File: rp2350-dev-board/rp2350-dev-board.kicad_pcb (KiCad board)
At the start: 2 copper layers, 40 parts, among them J1 USB_C_Receptacle_USB2.0_14P, J10 M1, J11 M1, J12 M1, J13 PWR_IN, J14 SWD, J2 M_EN, J3 HDMI_A, J8 1.47_IPS_LCD, J9 TMC_Volt_Select, SW1 BTN1, SW2 BTN1, SW3 BTN1, SW4 BTN1, SW5 BTN1, U4 L7805

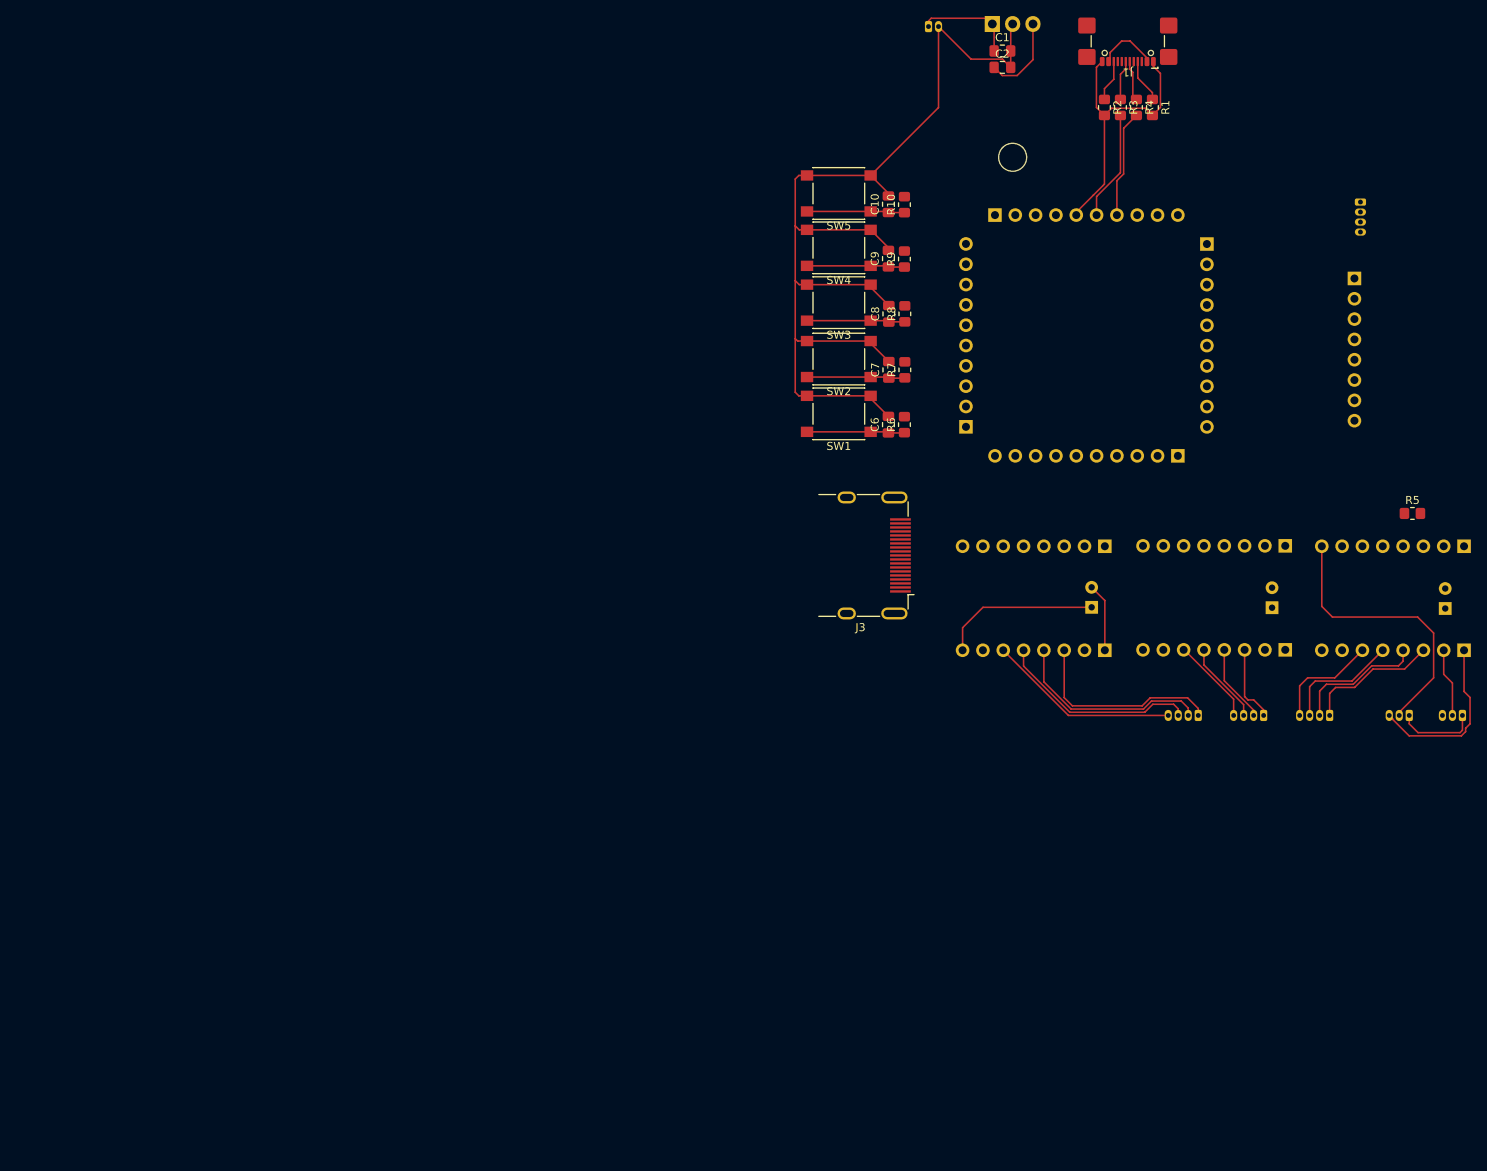
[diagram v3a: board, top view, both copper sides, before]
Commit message: feat(rp2350-devboard): copying tmc2209 and rp2350a-tempel into rp2350a devboard
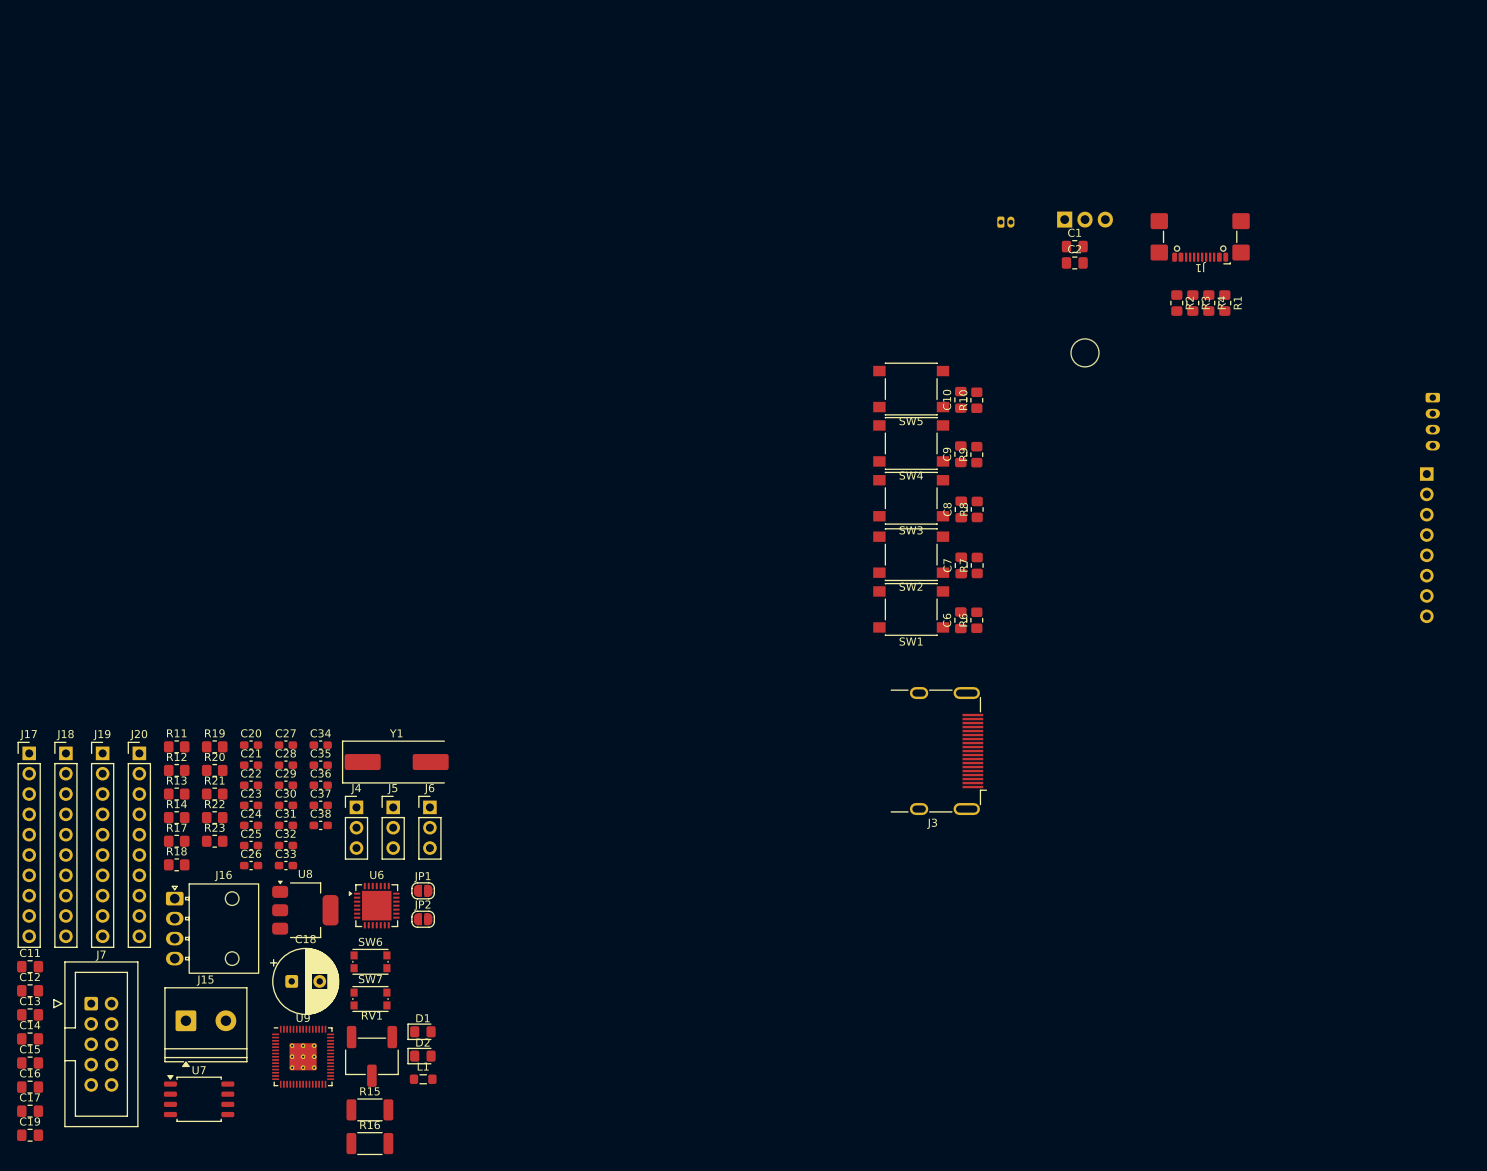
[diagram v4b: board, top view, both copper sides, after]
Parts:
- removed C3, C4, C5: 100uF, Capacitor_THT:CP_Radial_D6.3mm_P2.50mm
- removed J10, J11, J12: M1, Connector_Hirose:Hirose_DF13-04P-1.25DSA_1x04_P1.25mm_Vertical
- removed J2: M_EN, Connector_Hirose:Hirose_DF13-03P-1.25DSA_1x03_P1.25mm_Vertical
- removed J9: TMC_Volt_Select, Connector_Hirose:Hirose_DF13-03P-1.25DSA_1x03_P1.25mm_Vertical
- removed R5: 1K, Resistor_SMD:R_0805_2012Metric_Pad1.20x1.40mm_HandSolder
- removed U1, U2, U3: ~, rp2350-tempel-lib:TMC2209_MKS_V2
- removed U5: ~, rp2350-tempel-lib:RP2350_Tempel_Footprint
- added C11: 100nF, Capacitor_SMD:C_0805_2012Metric_Pad1.18x1.45mm_HandSolder, F.Cu at (32.7, 148.7)
- added C12: 100nF, Capacitor_SMD:C_0805_2012Metric_Pad1.18x1.45mm_HandSolder, F.Cu at (32.7, 151.7)
- added C13: 100nF, Capacitor_SMD:C_0805_2012Metric_Pad1.18x1.45mm_HandSolder, F.Cu at (32.7, 154.7)
- added C14: 100nF, Capacitor_SMD:C_0805_2012Metric_Pad1.18x1.45mm_HandSolder, F.Cu at (32.7, 157.7)
- added C15: 22nF/50V, Capacitor_SMD:C_0805_2012Metric_Pad1.18x1.45mm_HandSolder, F.Cu at (32.7, 160.7)
- added C16: 4.7uF, Capacitor_SMD:C_0805_2012Metric_Pad1.18x1.45mm_HandSolder, F.Cu at (32.7, 163.8)
- added C17: 4.7uF, Capacitor_SMD:C_0805_2012Metric_Pad1.18x1.45mm_HandSolder, F.Cu at (32.7, 166.8)
- added C18: 100uF, Capacitor_THT:CP_Radial_D8.0mm_P3.50mm, F.Cu at (65.4, 150.5)
- added C19: 2.2uF to 4.7uF/50V, Capacitor_SMD:C_0805_2012Metric_Pad1.18x1.45mm_HandSolder, F.Cu at (32.7, 169.8)
- added C20: 22uF, Capacitor_SMD:C_0603_1608Metric_Pad1.08x0.95mm_HandSolder, F.Cu at (60.3, 121.0)
- added C21: 100nF, Capacitor_SMD:C_0603_1608Metric_Pad1.08x0.95mm_HandSolder, F.Cu at (60.3, 123.5)
- added C22: 22uF, Capacitor_SMD:C_0603_1608Metric_Pad1.08x0.95mm_HandSolder, F.Cu at (60.3, 126.0)
- added C23: 12pF, Capacitor_SMD:C_0603_1608Metric_Pad1.08x0.95mm_HandSolder, F.Cu at (60.3, 128.5)
- added C24: 4.7uF, Capacitor_SMD:C_0603_1608Metric_Pad1.08x0.95mm_HandSolder, F.Cu at (60.3, 131.0)
- added C25: 4.7uF, Capacitor_SMD:C_0603_1608Metric_Pad1.08x0.95mm_HandSolder, F.Cu at (60.3, 133.6)
- added C26: 12pF, Capacitor_SMD:C_0603_1608Metric_Pad1.08x0.95mm_HandSolder, F.Cu at (60.3, 136.1)
- added C27: 4.7uF, Capacitor_SMD:C_0603_1608Metric_Pad1.08x0.95mm_HandSolder, F.Cu at (64.6, 121.0)
- added C28: 1uF, Capacitor_SMD:C_0603_1608Metric_Pad1.08x0.95mm_HandSolder, F.Cu at (64.6, 123.5)
- added C29: 4.7uF, Capacitor_SMD:C_0603_1608Metric_Pad1.08x0.95mm_HandSolder, F.Cu at (64.6, 126.0)
- added C30: 100nF, Capacitor_SMD:C_0603_1608Metric_Pad1.08x0.95mm_HandSolder, F.Cu at (64.6, 128.5)
- added C31: 100nF, Capacitor_SMD:C_0603_1608Metric_Pad1.08x0.95mm_HandSolder, F.Cu at (64.6, 131.0)
- added C32: 100nF, Capacitor_SMD:C_0603_1608Metric_Pad1.08x0.95mm_HandSolder, F.Cu at (64.6, 133.6)
- added C33: 100nF, Capacitor_SMD:C_0603_1608Metric_Pad1.08x0.95mm_HandSolder, F.Cu at (64.6, 136.1)
- added C34: 100nF, Capacitor_SMD:C_0603_1608Metric_Pad1.08x0.95mm_HandSolder, F.Cu at (69.0, 121.0)
- added C35: 100nF, Capacitor_SMD:C_0603_1608Metric_Pad1.08x0.95mm_HandSolder, F.Cu at (69.0, 123.5)
- added C36: 100nF, Capacitor_SMD:C_0603_1608Metric_Pad1.08x0.95mm_HandSolder, F.Cu at (69.0, 126.0)
- added C37: 100nF, Capacitor_SMD:C_0603_1608Metric_Pad1.08x0.95mm_HandSolder, F.Cu at (69.0, 128.5)
- added C38: 2u2F, Capacitor_SMD:C_0603_1608Metric_Pad1.08x0.95mm_HandSolder, F.Cu at (69.0, 131.0)
- added D1: DIAG, LED_SMD:LED_0805_2012Metric_Pad1.15x1.40mm_HandSolder, F.Cu at (81.8, 156.8)
- added D2: red, LED_SMD:LED_0805_2012Metric_Pad1.15x1.40mm_HandSolder, F.Cu at (81.8, 159.9)
- added J15: TMC2209_VIN, TerminalBlock_Phoenix:TerminalBlock_Phoenix_PT-1,5-2-5.0-H_1x02_P5.00mm_Horizontal, F.Cu at (52.1, 155.5)
- added J16: TMC2209_Conn, Connector_Molex:Molex_Nano-Fit_105313-xx04_1x04_P2.50mm_Horizontal, F.Cu at (50.7, 140.2)
- added J17: Conn_West, Connector_PinHeader_2.54mm:PinHeader_1x10_P2.54mm_Vertical, F.Cu at (32.5, 122.0)
- added J18: Conn_North, Connector_PinHeader_2.54mm:PinHeader_1x10_P2.54mm_Vertical, F.Cu at (37.1, 122.0)
- added J19: Conn_South, Connector_PinHeader_2.54mm:PinHeader_1x10_P2.54mm_Vertical, F.Cu at (41.7, 122.0)
- added J20: Conn_East, Connector_PinHeader_2.54mm:PinHeader_1x10_P2.54mm_Vertical, F.Cu at (46.3, 122.0)
- added J4: MS1, Connector_PinHeader_2.54mm:PinHeader_1x03_P2.54mm_Vertical, F.Cu at (73.5, 128.8)
- added J5: MS2, Connector_PinHeader_2.54mm:PinHeader_1x03_P2.54mm_Vertical, F.Cu at (78.0, 128.8)
- added J6: Spread, Connector_PinHeader_2.54mm:PinHeader_1x03_P2.54mm_Vertical, F.Cu at (82.6, 128.8)
- added J7: DriverConn, Connector_IDC:IDC-Header_2x05_P2.54mm_Vertical, F.Cu at (40.3, 153.3)
- added JP1: BRA, Jumper:SolderJumper-2_P1.3mm_Open_RoundedPad1.0x1.5mm, F.Cu at (81.8, 139.2)
- added JP2: BRB, Jumper:SolderJumper-2_P1.3mm_Open_RoundedPad1.0x1.5mm, F.Cu at (81.8, 142.8)
- added L1: 3.3uH, Inductor_SMD:L_0805_2012Metric_Pad1.05x1.20mm_HandSolder, F.Cu at (81.8, 162.8)
- added R11: 20K, Resistor_SMD:R_0805_2012Metric_Pad1.20x1.40mm_HandSolder, F.Cu at (51.0, 121.2)
- added R12: 100K, Resistor_SMD:R_0805_2012Metric_Pad1.20x1.40mm_HandSolder, F.Cu at (51.0, 124.2)
- added R13: 220, Resistor_SMD:R_0805_2012Metric_Pad1.20x1.40mm_HandSolder, F.Cu at (51.0, 127.1)
- added R14: 100K, Resistor_SMD:R_0805_2012Metric_Pad1.20x1.40mm_HandSolder, F.Cu at (51.0, 130.1)
- added R15: 120m 1W 2010, Resistor_SMD:R_2010_5025Metric, F.Cu at (75.1, 166.6)
- added R16: 120m 1W 2010, Resistor_SMD:R_2010_5025Metric, F.Cu at (75.1, 170.8)
- added R17: 10K, Resistor_SMD:R_0805_2012Metric_Pad1.20x1.40mm_HandSolder, F.Cu at (51.0, 133.0)
- added R18: 2K2, Resistor_SMD:R_0805_2012Metric_Pad1.20x1.40mm_HandSolder, F.Cu at (51.0, 136.0)
- added R19: 1K, Resistor_SMD:R_0805_2012Metric_Pad1.20x1.40mm_HandSolder, F.Cu at (55.7, 121.2)
- added R20: 33, Resistor_SMD:R_0805_2012Metric_Pad1.20x1.40mm_HandSolder, F.Cu at (55.7, 124.2)
- added R21: 1K, Resistor_SMD:R_0805_2012Metric_Pad1.20x1.40mm_HandSolder, F.Cu at (55.7, 127.1)
- added R22: 1K, Resistor_SMD:R_0805_2012Metric_Pad1.20x1.40mm_HandSolder, F.Cu at (55.7, 130.1)
- added R23: 1K, Resistor_SMD:R_0805_2012Metric_Pad1.20x1.40mm_HandSolder, F.Cu at (55.7, 133.0)
- added RV1: 10K, Potentiometer_SMD:Potentiometer_Bourns_3269W_Vertical, F.Cu at (75.4, 159.9)
- added SW6: BOOT SELECTOR, Button_Switch_SMD:SW_Push_1P1T_NO_CK_KMR2, F.Cu at (75.2, 148.1)
- added SW7: RST, Button_Switch_SMD:SW_Push_1P1T_NO_CK_KMR2, F.Cu at (75.2, 152.7)
- added U6: TMC2209-LA, Package_DFN_QFN:VQFN-28-1EP_5x5mm_P0.5mm_EP3.7x3.7mm, F.Cu at (76.0, 141.1)
- added U7: W25Q16JVSS, Package_SO:SOIC-8_5.3x5.3mm_P1.27mm, F.Cu at (53.8, 165.3)
- added U8: AMS1117-3.3, Package_TO_SOT_SMD:SOT-223-3_TabPin2, F.Cu at (67.1, 141.7)
- added U9: RP2350_60QFN, lib:RP2350-QFN-60-1EP_7x7_P0.4mm_EP3.4x3.4mm_ThermalVias, F.Cu at (66.8, 160.0)
- added Y1: 12Mhz HC49-SD, Crystal:Crystal_SMD_HC49-SD, F.Cu at (78.5, 123.1)
- J14: footprint Connector_Hirose:Hirose_DF13-04P-1.25DSA_1x04_P1.25mm_Vertical -> Connector_Molex:Molex_Micro-Latch_53253-0470_1x04_P2.00mm_Vertical
- moved R10 26.1 mm to (151.0, 77.9)
- moved C1 26.1 mm to (163.2, 58.7)
- moved C2 26.1 mm to (163.2, 60.7)
- moved C7 26.1 mm to (149.0, 98.6)
- moved C8 26.1 mm to (149.0, 91.5)
- moved J14 26.1 mm to (208.0, 77.6)
- moved J3 26.1 mm to (147.2, 121.8)
- moved J8 26.1 mm to (207.2, 87.1)
- moved R1 26.1 mm to (182.0, 65.8)
- moved R2 26.1 mm to (176.0, 65.8)
- moved R3 26.1 mm to (178.0, 65.8)
- moved R4 26.1 mm to (180.0, 65.8)
- moved R8 26.1 mm to (151.0, 91.5)
- moved SW4 26.1 mm to (142.8, 83.3)
- moved J1 26.1 mm to (178.9, 56.3)
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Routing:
- net GND: track 196.7 -> 0.00 mm
- net /M_EN: track 35.0 -> 0.00 mm
- net VS: track 32.6 -> 0.00 mm
- net Net-(J12-Pin_3): track 25.2 -> 0.00 mm
- net Net-(J12-Pin_2): track 25.1 -> 0.00 mm
- net Net-(J12-Pin_1): track 24.9 -> 0.00 mm
- net Net-(J12-Pin_4): track 24.0 -> 0.00 mm
- net +5V: track 18.3 -> 0.00 mm
- net Net-(J10-Pin_1): track 16.7 -> 0.00 mm
- net Net-(J10-Pin_2): track 16.4 -> 0.00 mm
- net Net-(J10-Pin_3): track 14.6 -> 0.00 mm
- net /USB_DM: track 13.7 -> 0.00 mm
- net /USB_DP: track 13.5 -> 0.00 mm
- net Net-(J10-Pin_4): track 13.4 -> 0.00 mm
- net /GPIO24: track 12.3 -> 0.00 mm
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
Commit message: feat(rp2350-dev-board): routing phase 1
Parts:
- C18, J15, J16, J17, J18, J19, J20, J4, J5, J6, J7: moved to B.Cu
- moved D2 277.6 mm to (-39.1, -90.0), turned to -90 degrees
- moved U8 259.1 mm to (-44.2, -92.3), turned to -90 degrees
- moved C20 243.6 mm to (-49.2, -96.6), turned to 90 degrees
- moved C22 241.5 mm to (-36.8, -95.1), turned to 90 degrees
- moved R19 236.1 mm to (-39.2, -94.9), turned to 90 degrees
- moved U7 217.6 mm to (-57.9, -21.4)
- moved SW6 211.9 mm to (-49.6, -23.2), turned to 180 degrees
- moved U9 211.3 mm to (-55.4, -12.4)
- moved C25 206.9 mm to (-35.2, -50.0)
- moved C27 206.9 mm to (-30.8, -62.5)
- moved L1 206.9 mm to (-13.7, -20.8)
- moved R20 206.9 mm to (-39.7, -59.4)
- moved R21 206.9 mm to (-39.7, -56.4)
- moved SW7 206.9 mm to (-20.2, -30.8)
- moved C24 206.9 mm to (-35.2, -52.5)
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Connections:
- J18 pad 2: /~{BOOTSEL} -> unconnected-(J18-Pin_2-Pad2)
- J18 pad 4: /USB_DP -> unconnected-(J18-Pin_4-Pad4)
- J18 pad 5: /USB_DM -> /~{BOOTSEL}
- J18 pad 8: /GPIO28_ADC2 -> /GPIO29_ADC3
- J18 pad 9: /GPIO29_ADC3 -> /GPIO28_ADC2
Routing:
- net +1V1: track 0.00 -> 167.6 mm, vias 0 -> 4
- net GND: track 0.00 -> 164.1 mm, vias 0 -> 2
- net +3.3V: track 0.00 -> 82.2 mm
- net VM: track 0.00 -> 54.6 mm
- net Net-(J16-Pin_2): track 0.00 -> 53.8 mm, vias 0 -> 2
- net Net-(J16-Pin_1): track 0.00 -> 47.3 mm, vias 0 -> 2
- net Net-(J16-Pin_3): track 0.00 -> 33.8 mm, vias 0 -> 2
- net Net-(J16-Pin_4): track 0.00 -> 25.6 mm
- net /SWCLK: track 0.00 -> 23.3 mm
- net /SWD: track 0.00 -> 21.3 mm
- net /GPIO17: track 0.00 -> 20.9 mm
- net /GPIO16: track 0.00 -> 20.3 mm
- net /GPIO15: track 0.00 -> 19.8 mm
- net /GPIO27_ADC1: track 0.00 -> 18.5 mm
- net /GPIO10: track 0.00 -> 18.1 mm
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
